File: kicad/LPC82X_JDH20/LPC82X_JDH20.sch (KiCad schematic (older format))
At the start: 2 parts

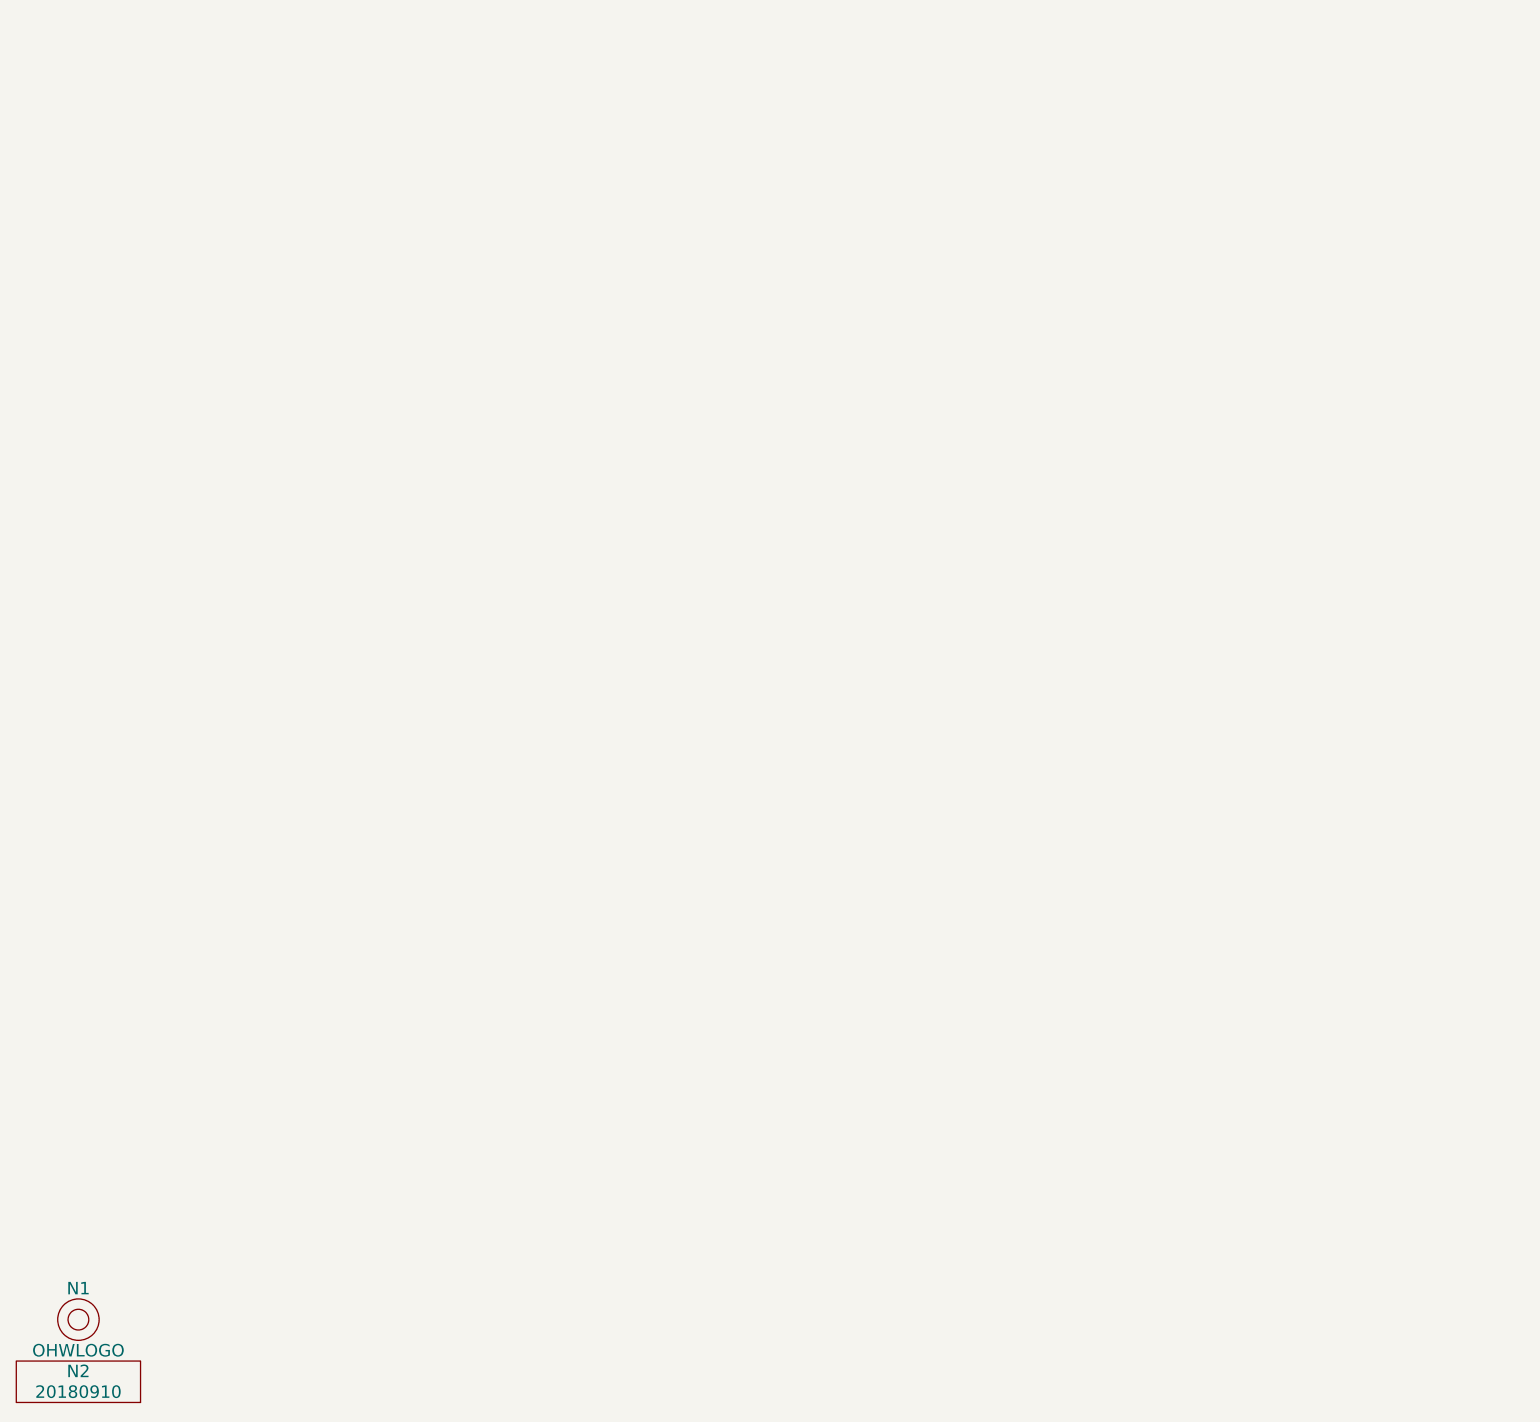
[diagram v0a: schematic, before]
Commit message: copied over schematic, updated libraries
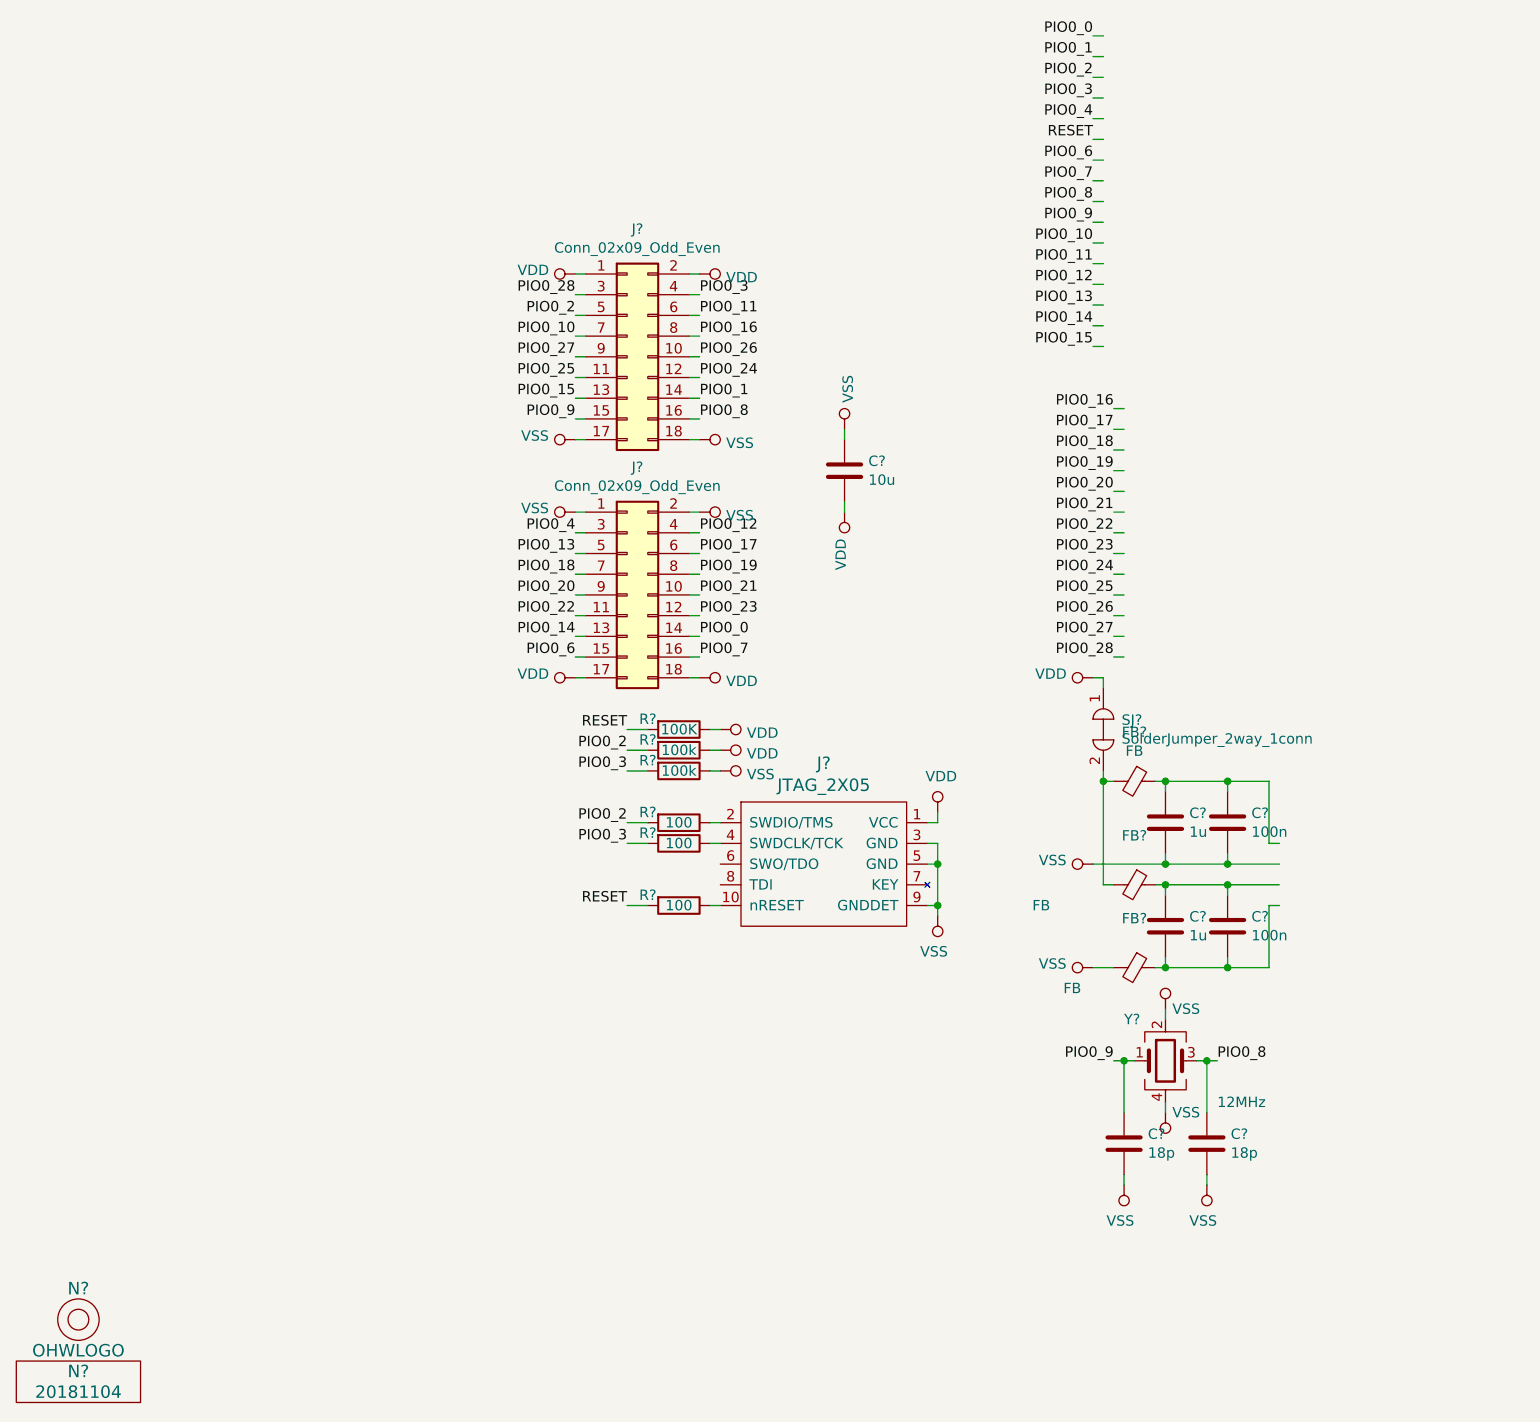
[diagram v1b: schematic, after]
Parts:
- removed N1: OHWLOGO, Symbols:OSHW-Symbol_6.7x6mm_SilkScreen, symbol SquantorLabels:OHWLOGO
- removed N2: 20180910, SquantorLabels:Label_version, symbol SquantorLabels:VYYYYMMDD
- added C? (x2): 100n, SquantorRcl:C_0402, symbol Device:C
- added C? (x2): 1u, SquantorRcl:C_0603, symbol Device:C
- added C?: 10u, SquantorRcl:C_0805, symbol Device:C
- added C? (x2): 18p, SquantorRcl:C_0402, symbol Device:C
- added FB? (x3): FB, SquantorRcl:C_0402, symbol Device:Ferrite_Bead_Small
- added J? (x2): Conn_02x09_Odd_Even, SquantorConnectors:Header-0254-2X09-H010, symbol Connector_Generic:Conn_02x09_Odd_Even
- added J?: JTAG_2X05, SquantorConnectors:Header-0127-2X05-H006, symbol SquantorConnectors:JTAG_2X05
- added N?: 20181104, SquantorLabels:Label_version, symbol SquantorLabels:VYYYYMMDD
- added N?: OHWLOGO, Symbols:OSHW-Symbol_6.7x6mm_SilkScreen, symbol SquantorLabels:OHWLOGO
- added R? (x3): 100, SquantorRcl:R_0402_hand, symbol Device:R
- added R?: 100K, SquantorRcl:R_0402_hand, symbol Device:R
- added R? (x2): 100k, SquantorRcl:R_0402_hand, symbol Device:R
- added SJ?: SolderJumper_2way_1conn, SquantorSpecial:solder_jumper_2way_conn, symbol SquantorSpecial:SolderJumper_2way_1conn
- added Y?: 12MHz, SquantorCrystal:Crystal_3225_4, symbol Device:Crystal_GND24
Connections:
- net labels added: PIO0_0, PIO0_1, PIO0_10, PIO0_11, PIO0_12, PIO0_13, PIO0_14, PIO0_15, PIO0_16, PIO0_17, PIO0_18, PIO0_19, PIO0_2, PIO0_20, PIO0_21, PIO0_22, PIO0_23, PIO0_24, PIO0_25, PIO0_26, PIO0_27, PIO0_28, PIO0_3, PIO0_4, PIO0_6, PIO0_7, PIO0_8, PIO0_9, RESET, VDD, VSS
- wire segments 0 -> 128

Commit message: schematic updates
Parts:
- removed J? (x2): Conn_02x09_Odd_Even, SquantorConnectors:Header-0254-2X09-H010, symbol Connector_Generic:Conn_02x09_Odd_Even
- added J1, J3: Conn_01x09, symbol Connector_Generic:Conn_01x09
- added M1: LPC824M201JDH20, SquantorNxp_SOT360, symbol SquantorNxp:LPC824M201JDH20
- gave numbers to parts that had none: 21
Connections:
- net labels removed: PIO0_16, PIO0_18, PIO0_19, PIO0_20, PIO0_21, PIO0_22, PIO0_24, PIO0_25, PIO0_26, PIO0_27, PIO0_28, PIO0_6, PIO0_7
- wire segments 128 -> 97
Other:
- moved on the sheet: C1

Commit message: completed schematic
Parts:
- J1, J3: footprint (none) -> SquantorConnectors:Header-0254-1X09-H010
- M1: footprint SquantorNxp_SOT360 -> SquantorIC:SOT360
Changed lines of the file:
@@
 EESchema Schematic File Version 4
 LIBS:LPC82X_JDH20-cache
-LIBS:LPC82X_JHI33_2layer-cache
 EELAYER 26 0
 EELAYER END
@@
 F 0 "M1" H 7078 5242 45  0000 L CNN
 F 1 "LPC824M201JDH20" H 7078 5158 45  0000 L CNN
-F 2 "SquantorNxp_SOT360" H 7180 4850 20  0001 C CNN
+F 2 "SquantorIC:SOT360" H 7180 4850 20  0001 C CNN
 F 3 "" H 7150 4700 60  0000 C CNN
 	1    6900 5200
@@
 F 0 "M1" H 7119 2992 45  0000 L CNN
 F 1 "LPC824M201JDH20" H 7119 2908 45  0000 L CNN
-F 2 "SquantorNxp_SOT360" H 6680 2750 20  0001 C CNN
+F 2 "SquantorIC:SOT360" H 6680 2750 20  0001 C CNN
 F 3 "" H 6650 2600 60  0000 C CNN
 	2    6400 3100
@@
 F 0 "J1" H 4169 2717 50  0000 C CNN
 F 1 "Conn_01x09" H 4169 2626 50  0000 C CNN
-F 2 "" H 4250 3250 50  0001 C CNN
+F 2 "SquantorConnectors:Header-0254-1X09-H010" H 4250 3250 50  0001 C CNN
 F 3 "~" H 4250 3250 50  0001 C CNN
 	1    4250 3250
@@
 F 0 "J3" H 4420 2625 50  0000 C CNN
 F 1 "Conn_01x09" H 4420 2716 50  0000 C CNN
-F 2 "" H 4500 3250 50  0001 C CNN
+F 2 "SquantorConnectors:Header-0254-1X09-H010" H 4500 3250 50  0001 C CNN
 F 3 "~" H 4500 3250 50  0001 C CNN
 	1    4500 3250

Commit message: updated version number
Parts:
- N2: value 20181104 -> 20181110
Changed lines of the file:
@@
 P 850 7700
 F 0 "N2" H 850 7800 60  0000 C CNN
-F 1 "20181104" H 850 7700 60  0000 C CNN
+F 1 "20181110" H 850 7700 60  0000 C CNN
 F 2 "SquantorLabels:Label_version" H 850 7700 60  0001 C CNN
 F 3 "" H 850 7700 60  0001 C CNN

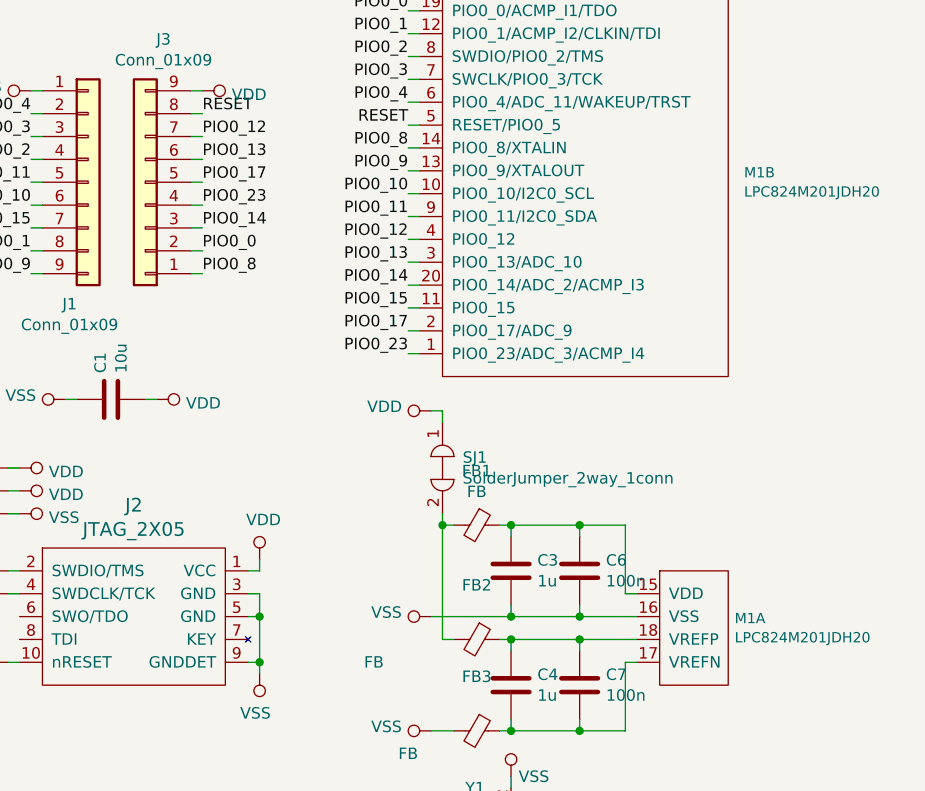
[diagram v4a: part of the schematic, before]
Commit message: updated LPC824 component
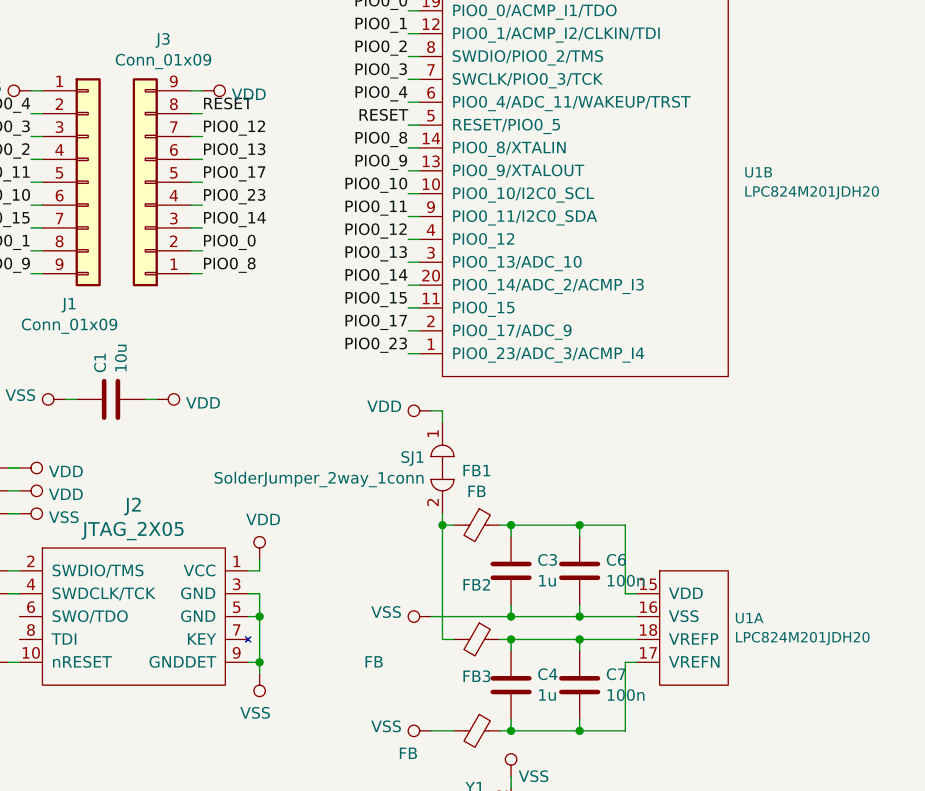
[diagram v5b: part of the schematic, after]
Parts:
- removed M1: LPC824M201JDH20, SquantorIC:SOT360, symbol SquantorNxp:LPC824M201JDH20
- added U1: LPC824M201JDH20, SquantorIC:SOT360, symbol SquantorNxp:LPC824M201JDH20
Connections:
- net PIO0_0: now also U1.19 (PIO0_0/ACMP_I1/TDO)
- net PIO0_1: now also U1.12 (PIO0_1/ACMP_I2/CLKIN/TDI)
- net PIO0_10: now also U1.10 (PIO0_10/I2C0_SCL)
- net PIO0_11: now also U1.9 (PIO0_11/I2C0_SDA)
- net PIO0_12: now also U1.4 (PIO0_12)
- net PIO0_13: now also U1.3 (PIO0_13/ADC_10)
- net PIO0_14: now also U1.20 (PIO0_14/ADC_2/ACMP_I3)
- net PIO0_15: now also U1.11 (PIO0_15)
- net PIO0_17: now also U1.2 (PIO0_17/ADC_9)
- net PIO0_2: now also U1.8 (SWDIO/PIO0_2/TMS)
- net PIO0_23: now also U1.1 (PIO0_23/ADC_3/ACMP_I4)
- net PIO0_3: now also U1.7 (SWCLK/PIO0_3/TCK)
- net PIO0_4: now also U1.6 (PIO0_4/ADC_11/WAKEUP/TRST)
- net PIO0_8: now also U1.14 (PIO0_8/XTALIN)
- net PIO0_9: now also U1.13 (PIO0_9/XTALOUT)
- net RESET: now also U1.5 (RESET/PIO0_5)
- net VSS: now also U1.16 (VSS)
- net at C4.1, C7.1, FB2.1: now also U1.18 (VREFP)
- net at C4.2, C7.2, FB3.1: now also U1.17 (VREFN)
- net at C3.1, C6.1, FB1.1: now also U1.15 (VDD)
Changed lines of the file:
@@
 U 1 1 5BDC2411
 P 5800 4500
-F 0 "SJ1" V 5754 4588 50  0000 L CNN
-F 1 "SolderJumper_2way_1conn" V 5845 4588 50  0000 L CNN
+F 0 "SJ1" V 5754 4423 50  0000 R CNN
+F 1 "SolderJumper_2way_1conn" V 5845 4423 50  0000 R CNN
 F 2 "SquantorSpecial:solder_jumper_2way_conn" H 5800 4500 50  0001 C CNN
 F 3 "" H 5800 4500 50  0001 C CNN
@@
 Wire Wire Line
 	5800 4250 5750 4250
-$Comp
-L SquantorNxp:LPC824M201JDH20 M1
-U 1 1 5BE0FC14
-P 6900 5200
-F 0 "M1" H 7078 5242 45  0000 L CNN
-F 1 "LPC824M201JDH20" H 7078 5158 45  0000 L CNN
-F 2 "SquantorIC:SOT360" H 7180 4850 20  0001 C CNN
-F 3 "" H 7150 4700 60  0000 C CNN
-	1    6900 5200
-	1    0    0    -1
-$EndComp
-$Comp
-L SquantorNxp:LPC824M201JDH20 M1
-U 2 1 5BE0FDBD
-P 6400 3100
-F 0 "M1" H 7119 2992 45  0000 L CNN
-F 1 "LPC824M201JDH20" H 7119 2908 45  0000 L CNN
-F 2 "SquantorIC:SOT360" H 6680 2750 20  0001 C CNN
-F 3 "" H 6650 2600 60  0000 C CNN
-	2    6400 3100
-	1    0    0    -1
-$EndComp
 $Comp
 L power:VSS #PWR0115
@@
 Wire Wire Line
 	4750 2950 4700 2950
+$Comp
+L SquantorNxp:LPC824M201JDH20 U1
+U 2 1 5BE68108
+P 6400 3100
+F 0 "U1" H 7119 2992 45  0000 L CNN
+F 1 "LPC824M201JDH20" H 7119 2908 45  0000 L CNN
+F 2 "SquantorIC:SOT360" H 6680 2750 20  0001 C CNN
+F 3 "" H 6650 2600 60  0000 C CNN
+	2    6400 3100
+	1    0    0    -1
+$EndComp
+$Comp
+L SquantorNxp:LPC824M201JDH20 U1
+U 1 1 5BE681B3
+P 6900 5200
+F 0 "U1" H 7078 5242 45  0000 L CNN
+F 1 "LPC824M201JDH20" H 7078 5158 45  0000 L CNN
+F 2 "SquantorIC:SOT360" H 7180 4850 20  0001 C CNN
+F 3 "" H 7150 4700 60  0000 C CNN
+	1    6900 5200
+	1    0    0    -1
+$EndComp
 $EndSCHEMATC

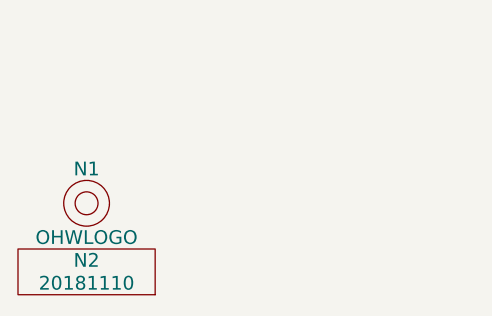
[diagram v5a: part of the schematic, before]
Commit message: small trace change, updated version number
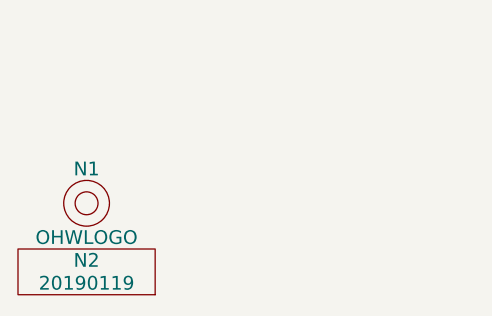
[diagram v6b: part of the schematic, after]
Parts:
- N2: value 20181110 -> 20190119
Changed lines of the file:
@@
 P 850 7700
 F 0 "N2" H 850 7800 60  0000 C CNN
-F 1 "20181110" H 850 7700 60  0000 C CNN
+F 1 "20190119" H 850 7700 60  0000 C CNN
 F 2 "SquantorLabels:Label_version" H 850 7700 60  0001 C CNN
 F 3 "" H 850 7700 60  0001 C CNN

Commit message: fixed mistake in microcontroller power, updated library component, added newer component library, rerouted
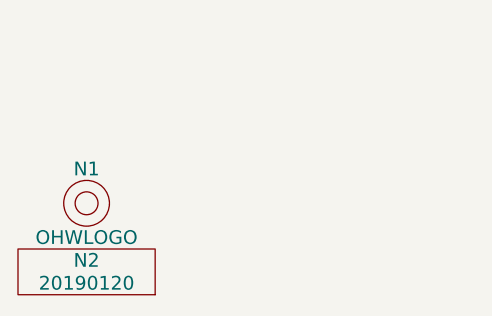
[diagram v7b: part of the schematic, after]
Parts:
- N2: value 20190119 -> 20190120
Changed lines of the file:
@@
 P 850 7700
 F 0 "N2" H 850 7800 60  0000 C CNN
-F 1 "20190119" H 850 7700 60  0000 C CNN
+F 1 "20190120" H 850 7700 60  0000 C CNN
 F 2 "SquantorLabels:Label_version" H 850 7700 60  0001 C CNN
 F 3 "" H 850 7700 60  0001 C CNN

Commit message: updated silkscreen
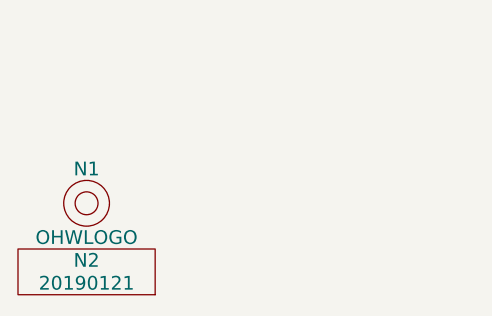
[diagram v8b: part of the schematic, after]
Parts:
- N2: value 20190120 -> 20190121
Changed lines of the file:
@@
 P 850 7700
 F 0 "N2" H 850 7800 60  0000 C CNN
-F 1 "20190120" H 850 7700 60  0000 C CNN
+F 1 "20190121" H 850 7700 60  0000 C CNN
 F 2 "SquantorLabels:Label_version" H 850 7700 60  0001 C CNN
 F 3 "" H 850 7700 60  0001 C CNN
